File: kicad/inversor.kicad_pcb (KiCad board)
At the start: 2 copper layers, 178 x 76 mm, 87 parts, among them J1 VCC, J10 To IGBTs, J2 PWM, J3 LCD 16x2, J4 MainFan, J5 380VFreed, J6 PRO_MINI_L, J8 PRO_MINI_R, J9 SPWM Driver Board, Q1 SSF6014D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

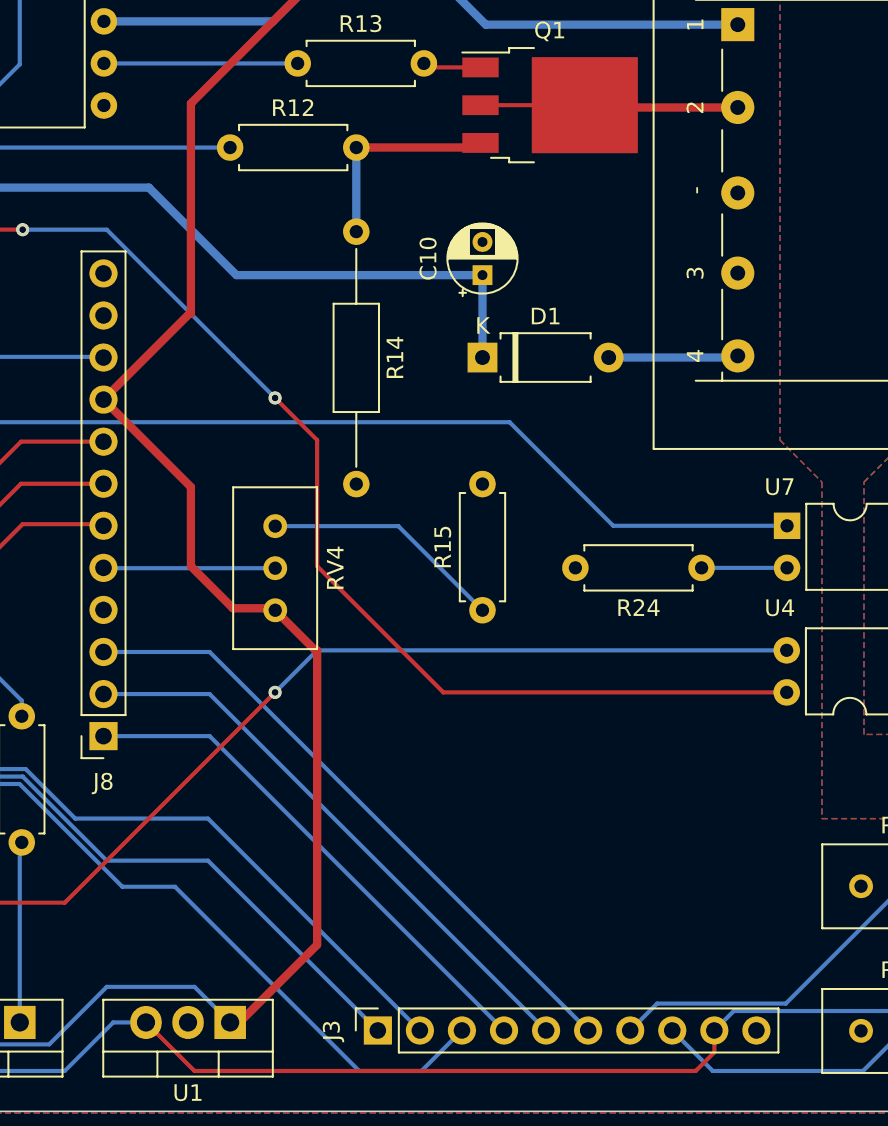
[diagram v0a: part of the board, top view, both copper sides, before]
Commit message: FIX: VCC Arduino 5v en lugar de VCC FIX: Divisor de tension para sensor de voltaje de batería con resistencia en la parte de vcc en lugar de gnd
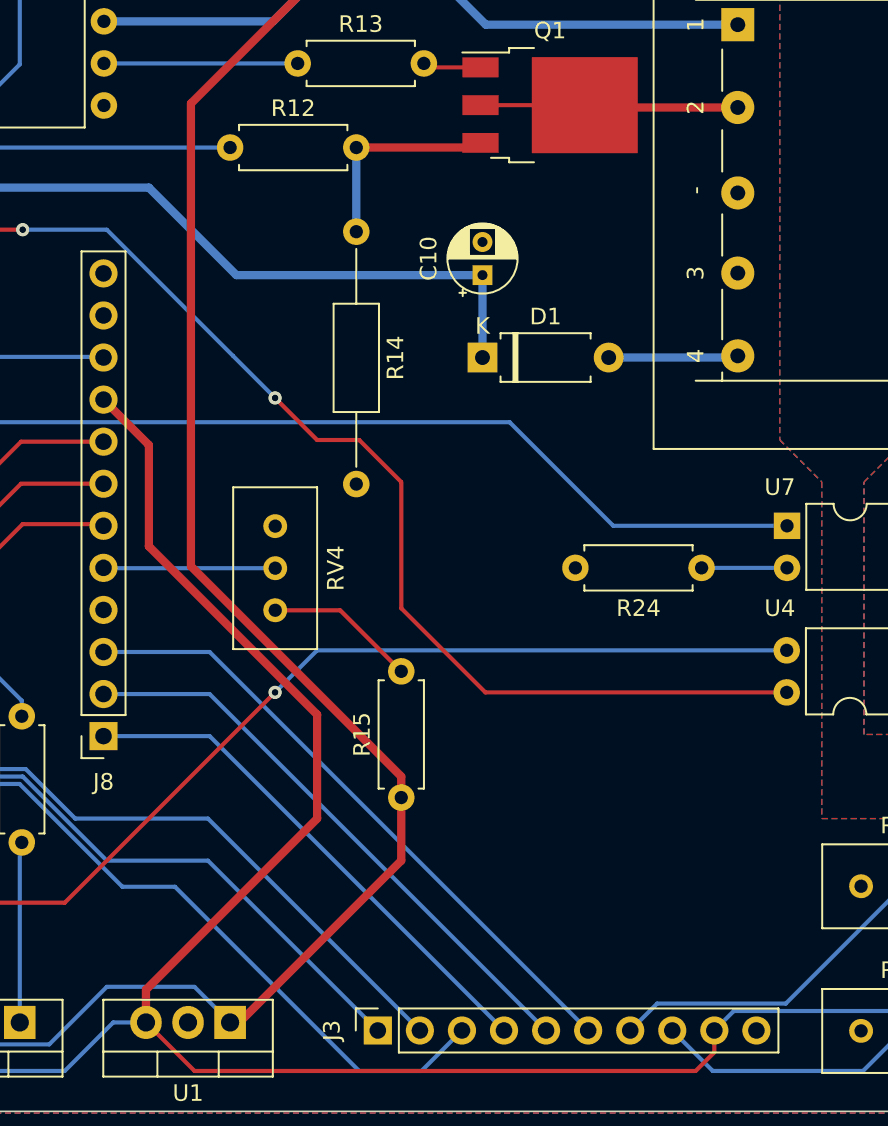
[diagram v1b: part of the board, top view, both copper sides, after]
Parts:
- moved R15 12.3 mm to (152.4, 82.5)
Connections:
- J8 pad 9: VCC -> +5V
- R15 pad 1: Net-(R15-Pad1) -> VCC
- R15 pad 2: GND -> Net-(R15-Pad2)
- RV4 pad 1: VCC -> Net-(R15-Pad2)
- RV4 pad 3: Net-(R15-Pad1) -> GND
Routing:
- net +5V: track 120.0 -> 167.2 mm
- net Net-(R15-Pad1): track 14.6 -> 0.00 mm
- net Net-(R15-Pad2): track 0.00 -> 9.14 mm
- net VCC: track 154.6 -> 152.9 mm

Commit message: Cambio Arduino por el ATMega328
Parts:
- removed J8: PRO_MINI_R, Connector_PinSocket_2.54mm:PinSocket_1x12_P2.54mm_Vertical
- added C14: 22pF, Capacitor_THT:C_Disc_D3.0mm_W1.6mm_P2.50mm, F.Cu at (111.8, 81.3)
- added C15: 22pF, Capacitor_THT:C_Disc_D3.0mm_W1.6mm_P2.50mm, F.Cu at (111.8, 66.0)
- added C16: 0.1uF, Capacitor_THT:C_Disc_D3.0mm_W1.6mm_P2.50mm, F.Cu at (129.5, 48.3)
- added C17: 250nF, Capacitor_THT:CP_Radial_D5.0mm_P2.50mm, F.Cu at (243.8, 88.9)
- added J7: LCD 16x2, Connector_PinSocket_2.54mm:PinSocket_1x10_P2.54mm_Vertical, F.Cu at (151.2, 96.5)
- added R36: 10K, Resistor_THT:R_Axial_DIN0207_L6.3mm_D2.5mm_P7.62mm_Horizontal, F.Cu at (129.5, 61.0)
- added U9: ATmega328-P, Package_DIP:DIP-28_W7.62mm, F.Cu at (118.1, 50.8)
- added Y1: 16Mhz, Crystal:Crystal_HC18-U_Vertical, F.Cu at (111.8, 76.0)
- J3: value LCD 16x2 -> ICSP; footprint Connector_PinSocket_2.54mm:PinSocket_1x10_P2.54mm_Vertical -> Connector_PinSocket_2.54mm:PinSocket_2x03_P2.54mm_Vertical
- J6: value PRO_MINI_L -> Serial FTDI; footprint Connector_PinSocket_2.54mm:PinSocket_1x12_P2.54mm_Vertical -> Connector_PinSocket_2.54mm:PinSocket_1x06_P2.54mm_Vertical
- moved J3 26.8 mm to (137.2, 73.7), turned to 0 degrees
- moved R18 16.4 mm to (114.3, 91.4)
- moved J6 15.9 mm to (134.6, 53.3)
- moved C9 15.2 mm to (111.9, 51.0)
- moved C6 12.6 mm to (106.6, 83.8), turned to 90 degrees
- moved R23 2.72 mm to (243.8, 76.2)
- moved C8 0.12 mm to (109.0, 58.4)
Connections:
- J3 pad 1: D8 -> D12-MISO
- J3 pad 2: D7 -> +5V
- J3 pad 3: D9 -> D13-SCK
- J3 pad 4: D10 -> D11-MOSI
- J3 pad 5: D11 -> DTR
- J3 pad 6: D12 -> GND
- J6 pad 1: TX0 -> GND
- J6 pad 2: RX1 -> +5V
- J6 pad 3: RST -> RX0
- J6 pad 4: GND -> TX0
- J6 pad 5: D2 -> DTR
- J6 pad 6: D3 -> GND
- RV2 pad 2: Net-(J3-Pad7) -> Net-(J7-Pad7)
- RV3 pad 2: Net-(J3-Pad8) -> Net-(J7-Pad8)
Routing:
- net D12-MISO: track 0.00 -> 59.0 mm
- net D11-MOSI: track 0.00 -> 52.9 mm
- net D12: track 38.7 -> 0.00 mm
- net DTR: track 0.00 -> 36.8 mm
- net D11: track 35.1 -> 0.00 mm
- net +5V: track 167.2 -> 192.6 mm
- net Net-(J7-Pad7): track 0.00 -> 20.1 mm
- net Net-(J3-Pad7): track 20.1 -> 0.00 mm
- net TX0: track 0.00 -> 19.8 mm
- net RX0: track 0.00 -> 19.5 mm
- net Net-(C16-Pad1): track 0.00 -> 17.6 mm
- net Net-(J7-Pad8): track 0.00 -> 16.0 mm
- net Net-(J3-Pad8): track 16.0 -> 0.00 mm
- net RST: track 15.5 -> 0.00 mm
- net D4: track 15.9 -> 29.8 mm
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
